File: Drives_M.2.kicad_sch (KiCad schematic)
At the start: 93 parts, among them IC1 AP62800SJ-7, IC2 AP62800SJ-7, J13 Bus_M.2_Socket_M, M1 M.2 Solder Nut, M10 M.2 Screw, M11 M.2 Solder Nut, M12 M.2 Solder Nut, M13 M.2 Solder Nut, M14 M.2 Solder Nut, M15 M.2 Screw, M16 M.2 Solder Nut, M17 M.2 Solder Nut, M18 M.2 Solder Nut, M19 M.2 Solder Nut, M2 M.2 Solder Nut, M20 M.2 Screw, M3 M.2 Solder Nut, M4 M.2 Solder Nut, M5 M.2 Screw, M6 M.2 Solder Nut, M7 M.2 Solder Nut, M8 M.2 Solder Nut, M9 M.2 Solder Nut, U7 ASM1184, U8 ASEK-32.768KHZ-L-R-T, U9 TMP102xxDRL

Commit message: Drives moved
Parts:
- removed C27, C28: 22u, symbol Device:C_Small
- removed C41, C42: 100n, symbol Device:C_Small
- removed C43, C44, C45, C46, C47, C48, C49, C50, C62: 22n, symbol Device:C_Small
- removed IC1, IC2: AP62800SJ-7, AP62800SJ7, symbol AP62800SJ-7:AP62800SJ-7
- removed L1, L2: 2u, symbol Device:L
- removed R10, R9: R, symbol Device:R
- removed R11, R12: 100K 1%, Resistor_SMD:R_0402_1005Metric, symbol Device:R
- removed R14, R15: 30.1k, symbol Device:R
- removed R17, R18: 137k, symbol Device:R
- removed R29: 10k, symbol Device:R
- removed U9: TMP102xxDRL, Package_TO_SOT_SMD:SOT-563, symbol Sensor_Temperature:TMP102xxDRL
- added C? (x2): 10u, symbol Device:C_Small
- added C? (x3): 47u, symbol Device:C_Small
- added C? (x2): 0.47u, symbol Device:C_Small
- added D? (x3): LED Green, LED_SMD:LED_0603_1608Metric, symbol Device:LED
- added IC?: LM61480Q3RPHRQ1, LM62460QRPHRQ1, symbol LM61480Q3RPHRQ1:LM61480Q3RPHRQ1
- added J? (x3): Bus_M.2_Socket_M, CM5IO:M.2 M Key socket, symbol CM5IO:Bus_M.2_Socket_M
- added L?: 2.2u, symbol Device:L
- added R? (x3): 1k, Resistor_SMD:R_0402_1005Metric, symbol Device:R
- added R?: 10k, symbol Device:R
- added TP? (x3): TestPoint, TestPoint:TestPoint_Pad_2.0x2.0mm, symbol Connector:TestPoint
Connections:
- net PCIe_RST is gone; now on net PCIE_nRST: U7.3 (RES_IN)
- net +5v: now also C?.1, C?.1, C?.2, C?.2, IC?.14 (VIN1), IC?.2 (VIN2)
- net GND: now also C?.1, C?.1, C?.2, C?.2, C?.2, C?.2, C?.2, IC?.1 (PGND2_1), IC?.12 (SYNC/_MODE), IC?.15 (PGND1_1), IC?.17 (PGND2_2), IC?.20 (PGND1_2), IC?.8 (AGND), J?.1 (GND), J?.1 (GND), J?.1 (GND), J?.15 (GND), J?.15 (GND), J?.15 (GND), J?.21 (GND), J?.21 (GND), J?.21 (GND), J?.27 (GND), J?.27 (GND), J?.27 (GND), J?.3 (GND), J?.3 (GND), J?.3 (GND), J?.33 (GND), J?.33 (GND), J?.33 (GND), J?.39 (GND), J?.39 (GND), J?.39 (GND), J?.45 (GND), J?.45 (GND), J?.45 (GND), J?.51 (GND), J?.51 (GND), J?.51 (GND), J?.57 (GND), J?.57 (GND), J?.57 (GND), J?.71 (GND), J?.71 (GND), J?.71 (GND), J?.73 (GND), J?.73 (GND), J?.73 (GND), J?.75 (GND), J?.75 (GND), J?.75 (GND), J?.9 (GND), J?.9 (GND), J?.9 (GND), J?.M1 (GND2230), J?.M1 (GND2230), J?.M1 (GND2230), J?.M2 (GND2242), J?.M2 (GND2242), J?.M2 (GND2242), J?.M3 (GND2260), J?.M3 (GND2260), J?.M3 (GND2260), J?.M4 (GND2280), J?.M4 (GND2280), J?.M4 (GND2280), J?.S1, J?.S1, J?.S1, J?.S2, J?.S2, J?.S2
- net M2_3v3: now also C?.1, C?.1, C?.1, D?.2 (A), D?.2 (A), D?.2 (A), IC?.5 (BIAS), IC?.7 (FB), J?.12 (3.3V), J?.12 (3.3V), J?.12 (3.3V), J?.14 (3.3V), J?.14 (3.3V), J?.14 (3.3V), J?.16 (3.3V), J?.16 (3.3V), J?.16 (3.3V), J?.18 (3.3V), J?.18 (3.3V), J?.18 (3.3V), J?.2 (3.3V), J?.2 (3.3V), J?.2 (3.3V), J?.4 (3.3V), J?.4 (3.3V), J?.4 (3.3V), J?.70 (3.3V), J?.70 (3.3V), J?.70 (3.3V), J?.72 (3.3V), J?.72 (3.3V), J?.72 (3.3V), J?.74 (3.3V), J?.74 (3.3V), J?.74 (3.3V), L?.2, R?.2
- net PCIE_nCLKREQ: now also J13.52 (~{CLKREQ}), J?.52 (~{CLKREQ}), J?.52 (~{CLKREQ}), J?.52 (~{CLKREQ})
- net PCIE_nWAKE: now also J13.54 (~{PEWAKE}), J?.54 (~{PEWAKE}), J?.54 (~{PEWAKE}), J?.54 (~{PEWAKE})
- net PCIe_CLK_N_1: now also J13.53 (REFCLKn), J?.53 (REFCLKn), J?.53 (REFCLKn), J?.53 (REFCLKn)
- net PCIe_CLK_P_1: now also J13.55 (REFCLKp), J?.55 (REFCLKp), J?.55 (REFCLKp), J?.55 (REFCLKp)
- net PCIe_RST_M2: now also J13.50 (~{PERST}), J?.50 (~{PERST}), J?.50 (~{PERST}), J?.50 (~{PERST})
- net SUSCLK: now reaches J13.68 (SUSCLK), U8.3 (Out)
- net SUSCLK: now also J?.68 (SUSCLK), J?.68 (SUSCLK), J?.68 (SUSCLK)
- new net: IC?.16 (SW), IC?.3 (RBOOT), IC?.4 (CBOOT), L?.1
- new net: J?.10 (DAS/~{DSS}/~{LED1}), R?.2 (x3)
- new net: D?.1 (K), R?.1, TP?.1 (x2)
- new net: D?.1 (K), R?.1
- new net: IC?.10 (~{RESET_1}), IC?.19 (~{RESET_2}), R?.1
- new net: IC?.11 (SPSP), IC?.18 (VCC_2), IC?.6 (VCC_1), IC?.9 (RT)
- new net PCIE_PWR_EN: IC?.13 (EN)
- no-connect marks 17 -> 56
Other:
- moved on the sheet: C21, C22, C23, C24, C25, C26, C29, C30, C31, C32, C33, C34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

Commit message: Sheet name edit and changed to net labels
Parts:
- removed C57, C58, C59, C60: 100nF, Capacitor_SMD:C_0402_1005Metric, symbol Device:C
- added C71, C72, C73, C74: 100nF, Capacitor_SMD:C_0402_1005Metric, symbol Device:C
- C48: renamed from C22; value 100nF -> 100n
- C51: renamed from C25; value 100nF -> 100n
- C54: renamed from C30; value 100nF -> 100n
- C57: renamed from C33; value 100nF -> 100n
- C60: renamed from C36; value 100nF -> 100n
- gave numbers to parts that had none: 22
- renumbered C21 to C47, C23 to C49, C24 to C50, C26 to C52, C29 to C53, C31 to C55, C32 to C56, C34 to C58, C35 to C59, C37 to C61, C38 to C62, C39 to C63, C40 to C64, C51 to C65, C52 to C66, C53 to C67, C54 to C68, C55 to C69, C56 to C70, C61 to C77, D5 to D6, J13 to J10, M6 to M1, M20 to M10, M1 to M11, M2 to M12, M3 to M13, M4 to M14, M5 to M15, M11 to M16, M12 to M17, M13 to M18, M14 to M19, M7 to M2, M15 to M20, M8 to M3, M9 to M4, M10 to M5, M16 to M6, M17 to M7, M18 to M8, M19 to M9, R13 to R27, R16 to R28, R19 to R29, R20 to R30, R21 to R31, R22 to R32, R23 to R33, R24 to R34, R25 to R35, R26 to R36, R27 to R37, R28 to R38, TP3 to TP4, U8 to U10, U7 to U9
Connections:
- net PCIE_TX_N: now also C74.1
- net PCIE_TX_P: now also C73.1
- net PCIe_CLK_N_1: no longer J11.53 (REFCLKn), J12.53 (REFCLKn), J13.53 (REFCLKn)
- net PCIe_CLK_N_2: now also J11.53 (REFCLKn)
- net PCIe_CLK_N_4: now also J12.53 (REFCLKn), J13.53 (REFCLKn)
- net PCIe_CLK_P_1: no longer J11.55 (REFCLKp), J12.55 (REFCLKp), J13.55 (REFCLKp)
- net PCIe_CLK_P_2: now also J11.55 (REFCLKp)
- net PCIe_CLK_P_4: now also J12.55 (REFCLKp), J13.55 (REFCLKp)
- net PCIe_RX_N_1: now also J10.41 (PETn0)
- net PCIe_RX_N_2: now also J11.41 (PETn0)
- net PCIe_RX_N_3: now also J12.41 (PETn0)
- net PCIe_RX_N_4: now also J13.41 (PETn0)
- net PCIe_RX_P_1: now also J10.43 (PETp0)
- net PCIe_RX_P_2: now also J11.43 (PETp0)
- net PCIe_RX_P_3: now also J12.43 (PETp0)
- net PCIe_RX_P_4: now also J13.43 (PETp0)
- net PCIe_TX_N_1: now also J10.47 (PERn0)
- net PCIe_TX_N_2: now also J11.47 (PERn0)
- net PCIe_TX_N_3: now also J12.47 (PERn0)
- net PCIe_TX_N_4: now also J13.47 (PERn0), C72.1
- net PCIe_TX_P_1: now also J10.49 (PERp0)
- net PCIe_TX_P_2: now also J11.49 (PERp0)
- net PCIe_TX_P_3: now also J12.49 (PERp0)
- net PCIe_TX_P_4: now also J13.49 (PERp0), C71.1
- net at U9.58 (TXN_4): now also C72.2
- net at U9.54 (TXP_IN): now also C73.2
- net at U9.55 (TXN_IN): now also C74.2
- net at U9.57 (TXP_4): now also C71.2
- net PCIe_RST_M2 renamed ~{PERST}

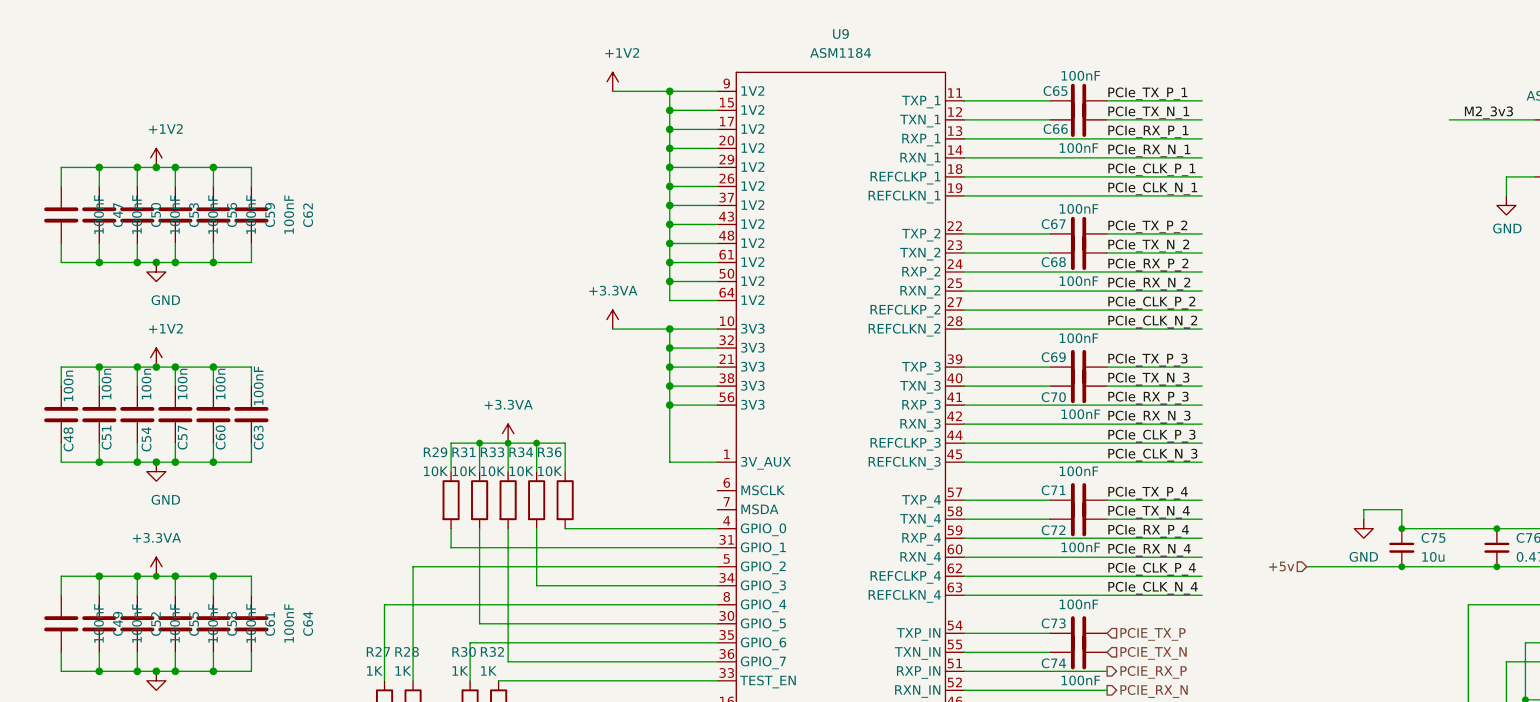
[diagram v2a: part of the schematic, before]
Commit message: Notation changed on M.2 Sheet
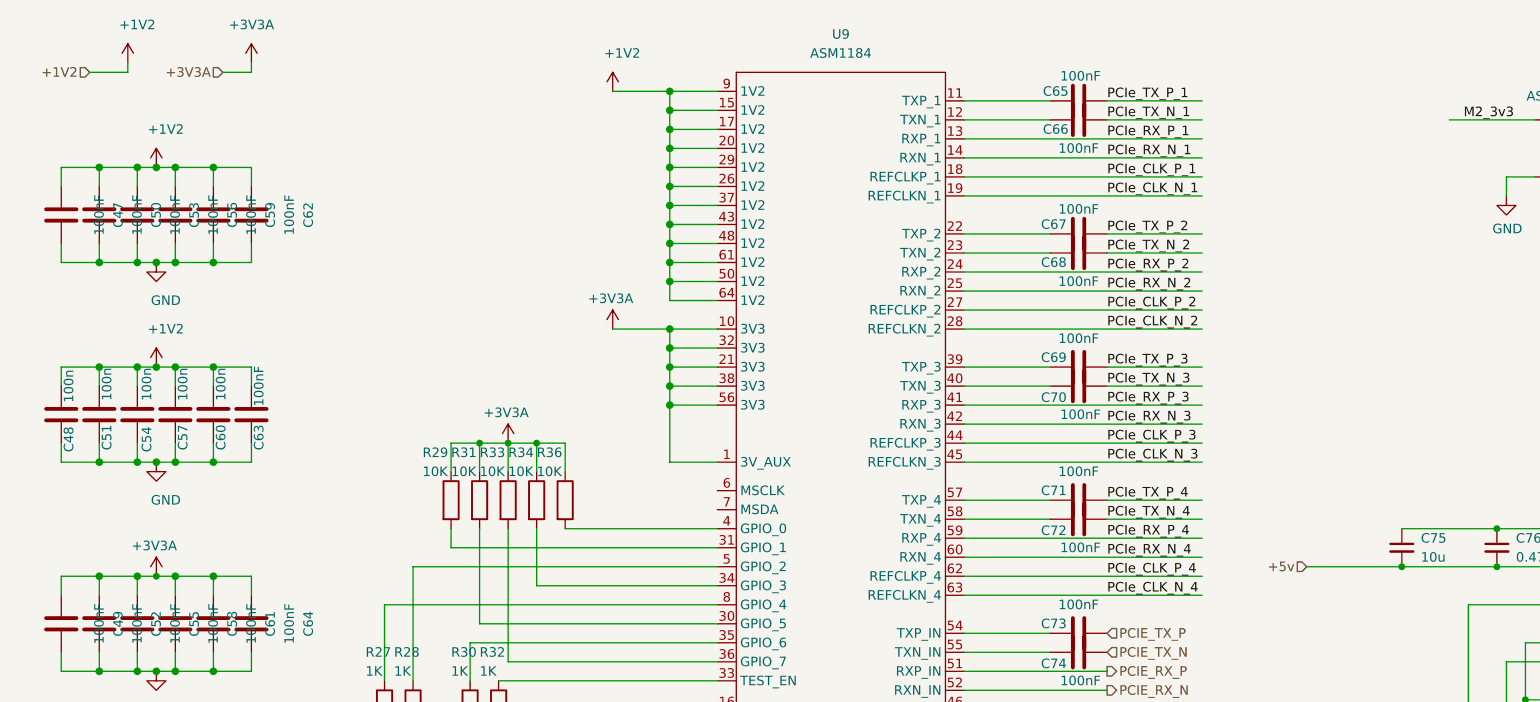
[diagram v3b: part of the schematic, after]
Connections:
- net +3.3VA renamed +3V3A

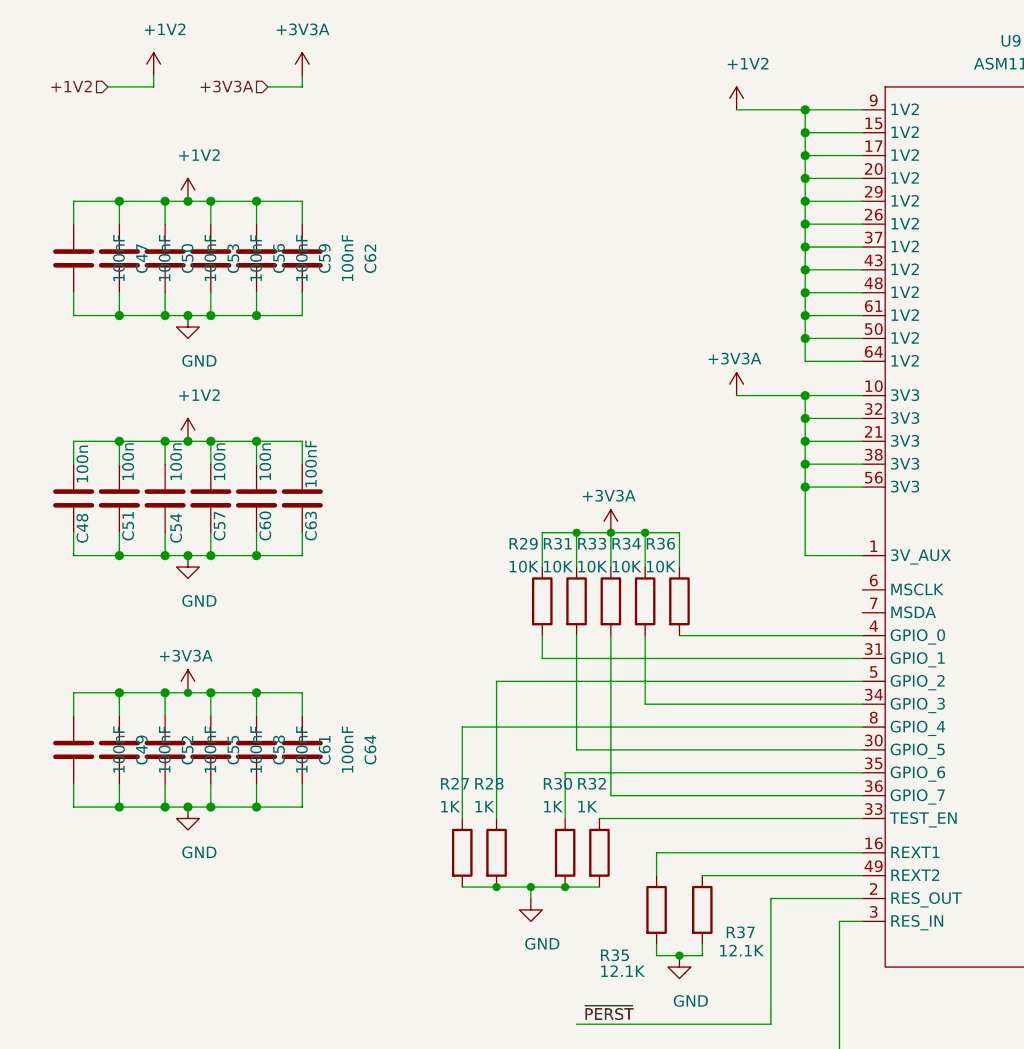
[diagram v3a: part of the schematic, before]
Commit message: Started Ethernet design
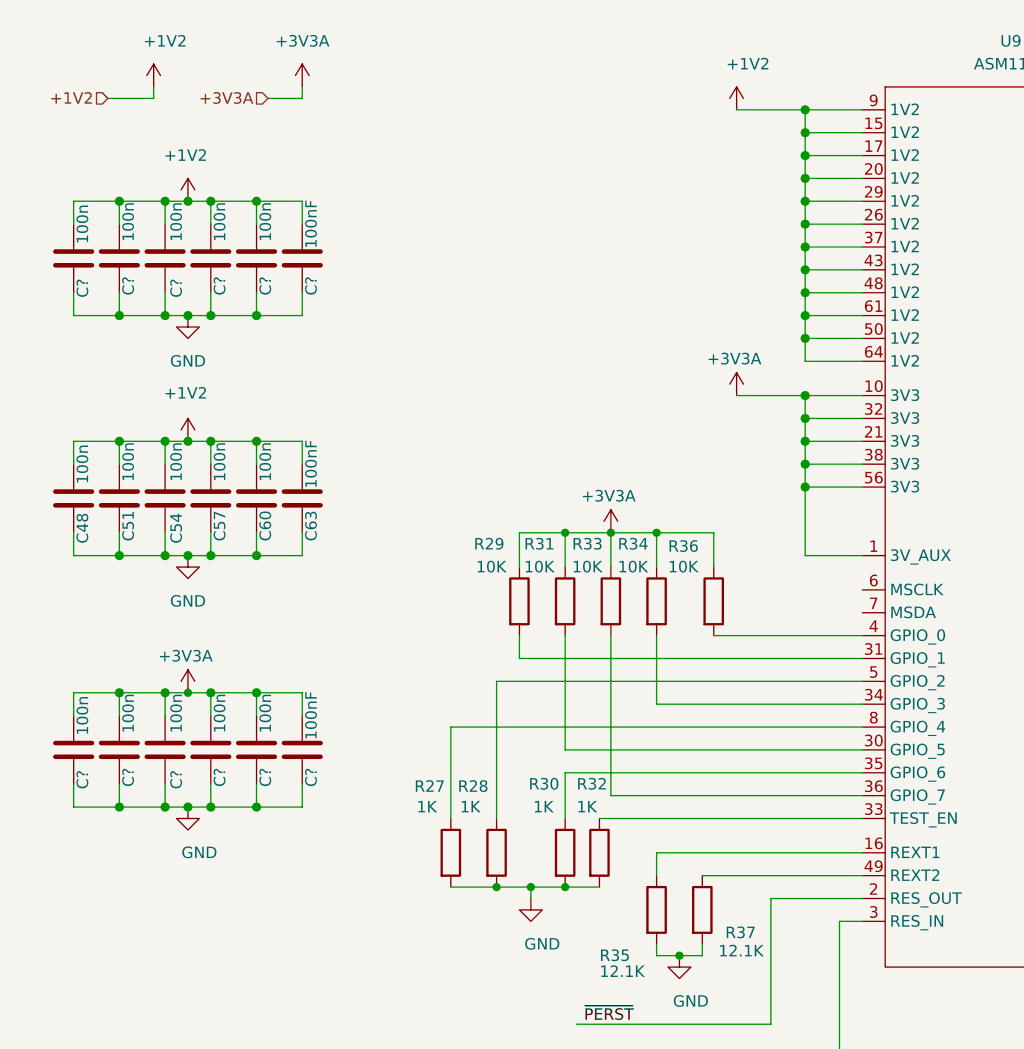
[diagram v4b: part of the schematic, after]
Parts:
- removed C47, C49, C50, C52, C53, C55, C56, C58, C59, C61, C62, C64: 100nF, Capacitor_SMD:C_0402_1005Metric, symbol Device:C
- added C? (x10): 100n, Capacitor_SMD:C_0402_1005Metric, symbol Device:C
- added C? (x2): 100nF, Capacitor_SMD:C_0402_1005Metric, symbol Device:C
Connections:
- net +1V2: now also C?.1, C?.1, C?.1, C?.1, C?.1, C?.1
- net +3V3A: now also C?.1, C?.1, C?.1, C?.1, C?.1, C?.1
- net GND: now also C?.2, C?.2, C?.2, C?.2, C?.2, C?.2, C?.2, C?.2, C?.2, C?.2, C?.2, C?.2
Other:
- moved on the sheet: R27, R29, R31, R34, R36
